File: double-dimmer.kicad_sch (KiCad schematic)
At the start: 4 parts, among them J1 Netzspannung, J2 Screw_Terminal_01x05

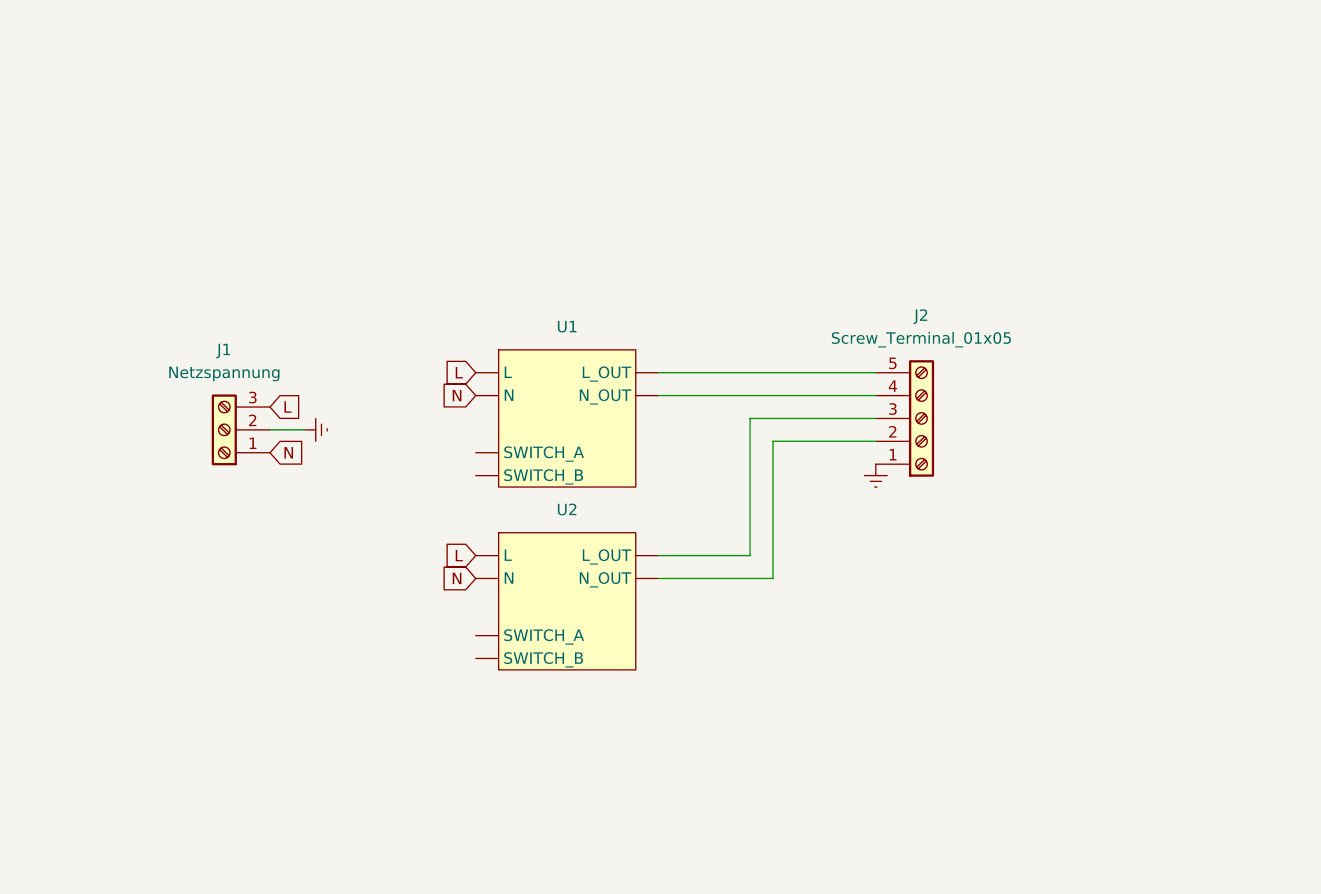
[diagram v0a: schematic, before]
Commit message: Add screenshot and update missing schematic
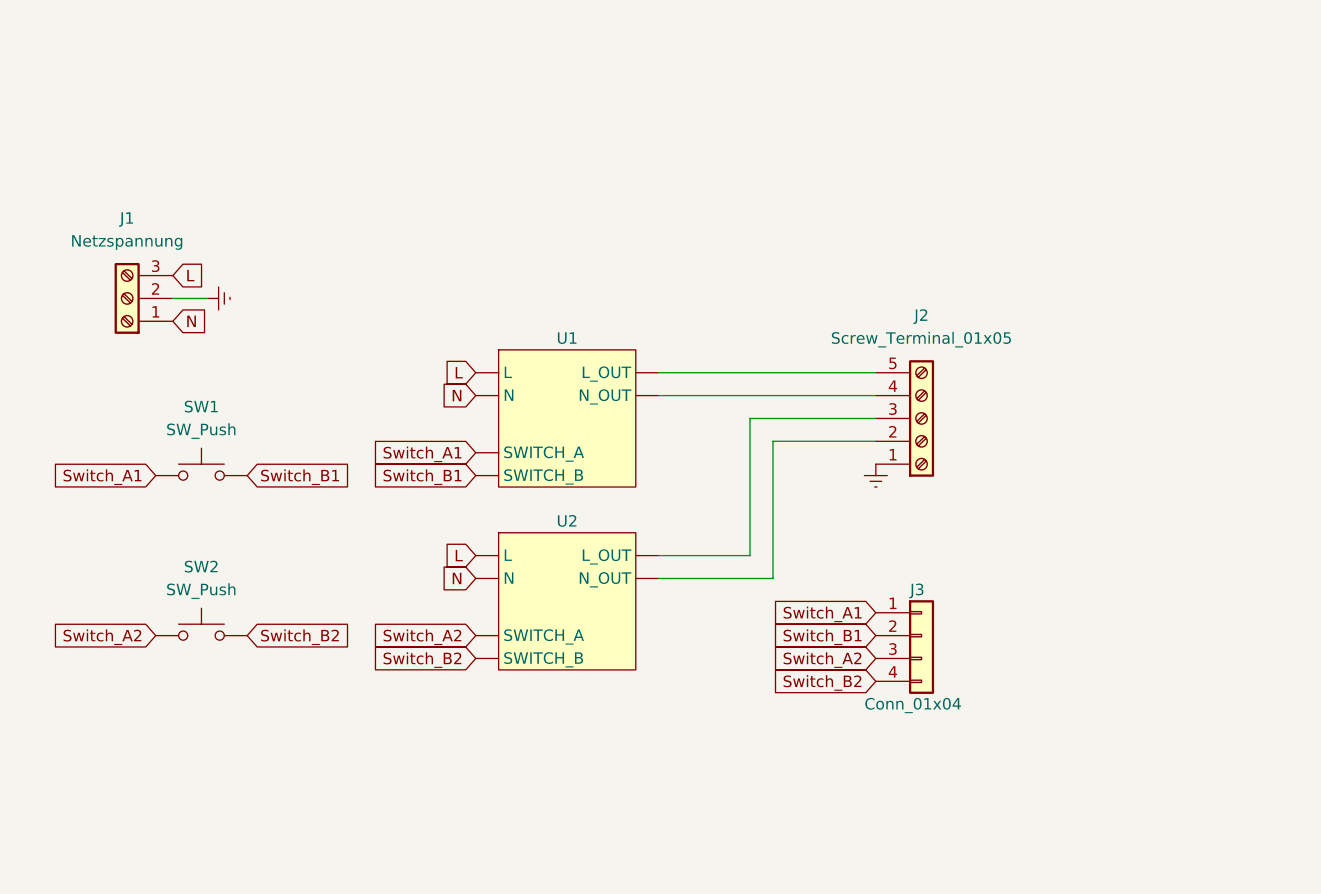
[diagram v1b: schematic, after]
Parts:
- added J3: Conn_01x04, Connector_PinHeader_2.00mm:PinHeader_1x04_P2.00mm_Vertical, symbol Connector_Generic:Conn_01x04
- added SW1, SW2: SW_Push, symbol Switch:SW_Push
- J1: footprint (none) -> TerminalBlock_Phoenix:TerminalBlock_Phoenix_MKDS-1,5-3-5.08_1x03_P5.08mm_Horizontal
- J2: footprint (none) -> TerminalBlock_Phoenix:TerminalBlock_Phoenix_MKDS-1,5-5-5.08_1x05_P5.08mm_Horizontal
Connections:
- net Switch_B2: now reaches U2. (SWITCH_B)
- net Switch_B2: now also J3.4 (Pin_4), SW2.1
- net Switch_B1: now reaches U1. (SWITCH_B)
- net Switch_B1: now also J3.2 (Pin_2), SW1.1
- new net Switch_A1: J3.1 (Pin_1), SW1.2, U1. (SWITCH_B)
- new net Switch_A2: J3.3 (Pin_3), SW2.2, U2. (SWITCH_B)
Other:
- moved on the sheet: J1

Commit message: Update dimmer footprint and add fuse and a switch
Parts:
- added F1: Fuse, Fuse:Fuseholder_Cylinder-5x20mm_Schurter_0031_8201_Horizontal_Open, symbol Device:Fuse
- added SW1: ButtonA, pts636:pts636, symbol Switch:SW_Push
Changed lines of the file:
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@@
+    )
+  )
+  (symbol (lib_id "Device:Fuse") (at 35.56 40.64 90) (unit 1)
+    (in_bom yes) (on_board yes) (dnp no) (fields_autoplaced)
+    (property "Reference" "F1" (at 35.56 34.29 90)
+      (effects (font (size 1.27 1.27)))
+    )
+    (property "Value" "Fuse" (at 35.56 36.83 90)
+      (effects (font (size 1.27 1.27)))
+    )
+    (property "Footprint" "Fuse:Fuseholder_Cylinder-5x20mm_Schurter_0031_8201_Horizontal_Open" (at 35.56 42.418 90)
+      (effects (font (size 1.27 1.27)) hide)
+    )
+    (property "Datasheet" "~" (at 35.56 40.64 0)
+      (effects (font (size 1.27 1.27)) hide)
+    )
+    (property "Price" "2.5" (at 35.56 40.64 0)
+      (effects (font (size 1.27 1.27)) hide)
+    )
+    (property "URL" "" (at 35.56 40.64 0)
+      (effects (font (size 1.27 1.27)) hide)
+    )
+    (pin "1")
+    (pin "2")
+    (instances
+      (project "double-dimmer"
+        (path "/a2cfefb5-9b8f-4ea6-9600-ced2f5c1dc62"
+          (reference "F1") (unit 1)
+        )
+      )
     )
   )
@@
         )
       )
+    )
+  )
+  (symbol (lib_id "Switch:SW_Push") (at 50.8 40.64 0) (unit 1)
+    (in_bom yes) (on_board yes) (dnp no)
+    (property "Reference" "SW1" (at 50.8 36.83 0)
+      (effects (font (size 1.27 1.27)))
+    )
+    (property "Value" "ButtonA" (at 68.58 40.64 0)
+      (effects (font (size 1.27 1.27)) hide)
+    )
+    (property "Footprint" "pts636:pts636" (at 50.8 35.56 0)
+      (effects (font (size 1.27 1.27)) hide)
+    )
+    (property "Datasheet" "~" (at 50.8 35.56 0)
+      (effects (font (size 1.27 1.27)) hide)
+    )
+    (property "Price" ".5" (at 50.8 40.64 0)
+      (effects (font (size 1.27 1.27)) hide)
+    )
+    (property "URL" "https://www.digikey.ch/en/products/detail/c-k/PTS636-SL43-LFS/10071714" (at 50.8 40.64 0)
+      (effects (font (size 1.27 1.27)) hide)
+    )
+    (pin "1")
+    (pin "2")
+    (instances
+      (project "double-dimmer"
+        (path "/a2cfefb5-9b8f-4ea6-9600-ced2f5c1dc62"
+          (reference "SW1") (unit 1)
+        )
+      )

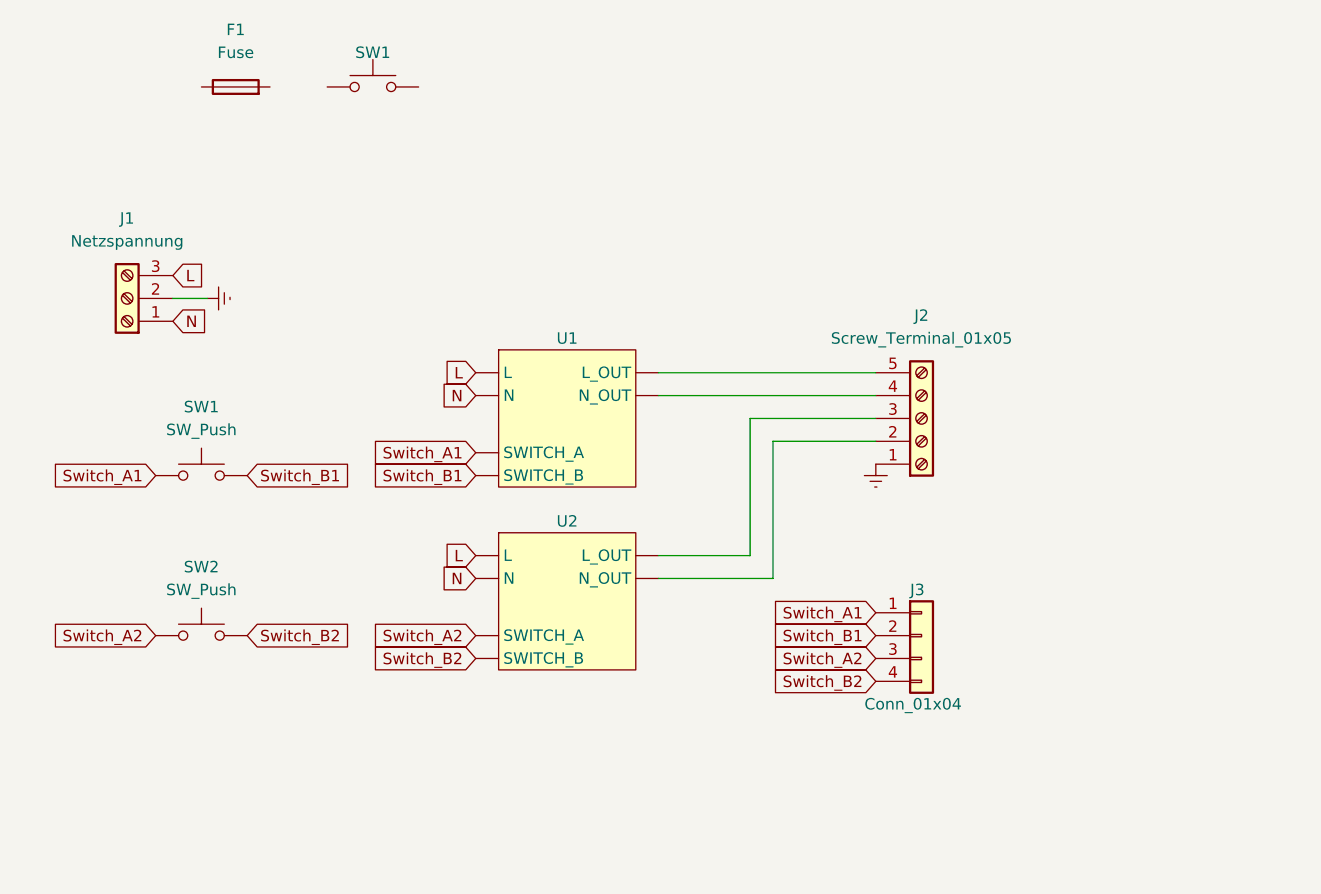
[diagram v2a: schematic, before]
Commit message: Update dimmer footprint and symbol
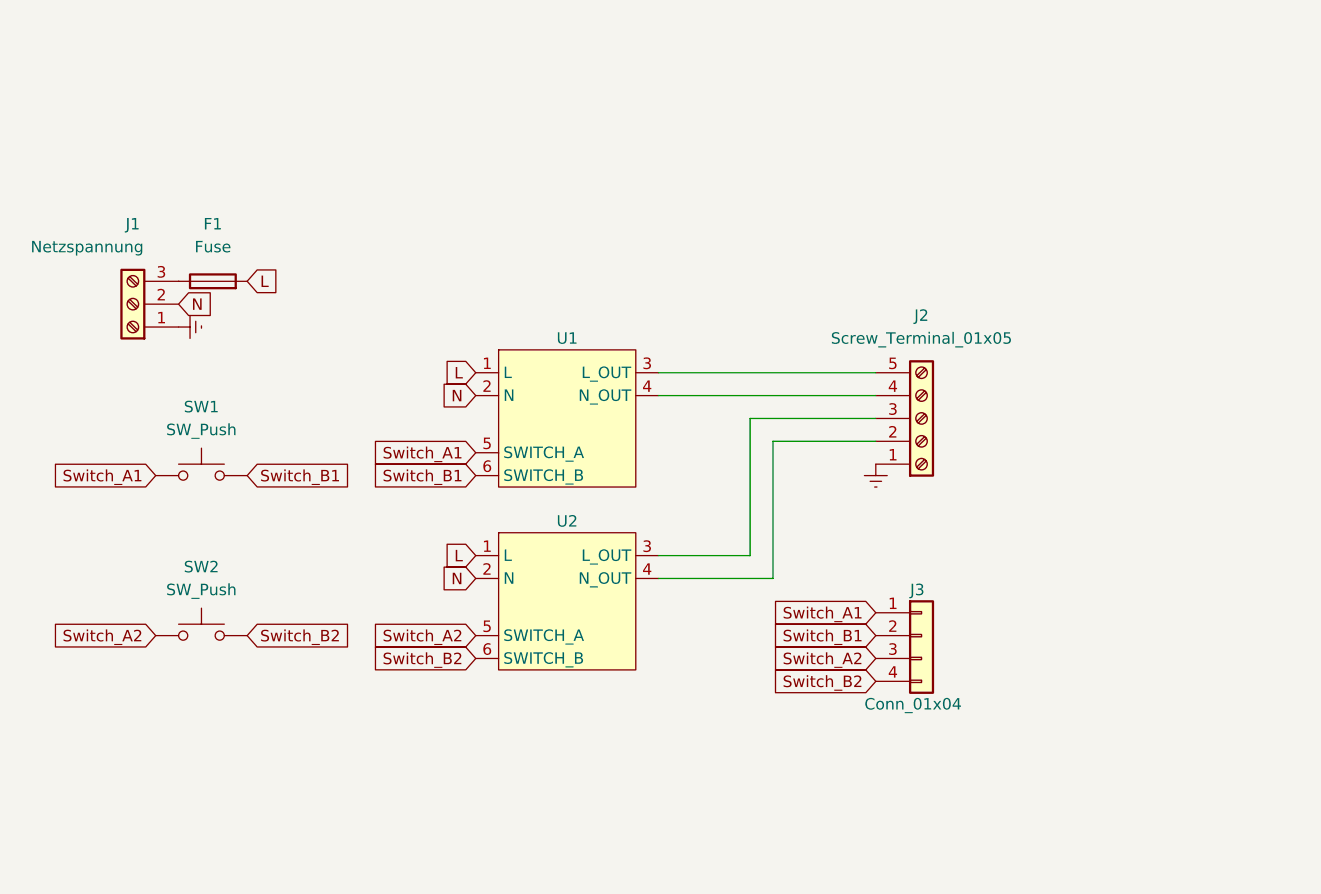
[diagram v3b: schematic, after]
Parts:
- removed SW1: ButtonA, pts636:pts636, symbol Switch:SW_Push
- J3: footprint Connector_PinHeader_2.00mm:PinHeader_1x04_P2.00mm_Vertical -> Connector_PinHeader_2.54mm:PinHeader_1x04_P2.54mm_Vertical
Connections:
- net Earth: now also J1.1 (Pin_1); no longer J1.2 (Pin_2)
- net L: now also F1.2, U1.1 (L), U2.1 (L); no longer J1.3 (Pin_3), U1. (SWITCH_B), U2. (SWITCH_B)
- net N: now also J1.2 (Pin_2), U1.2 (N), U2.2 (N); no longer J1.1 (Pin_1), U1. (SWITCH_B), U2. (SWITCH_B)
- net Switch_A1: now also U1.5 (SWITCH_A); no longer U1. (SWITCH_B)
- net Switch_A2: now also U2.5 (SWITCH_A); no longer U2. (SWITCH_B)
- net Switch_B1: now also U1.6 (SWITCH_B); no longer U1. (SWITCH_B)
- net Switch_B2: now also U2.6 (SWITCH_B); no longer U2. (SWITCH_B)
- net at J2.2 (Pin_2): now also U2.4 (N_OUT); no longer U2. (SWITCH_B)
- net at J2.3 (Pin_3): now also U2.3 (L_OUT); no longer U2. (SWITCH_B)
- net at J2.4 (Pin_4): now also U1.4 (N_OUT); no longer U1. (SWITCH_B)
- net at J2.5 (Pin_5): now also U1.3 (L_OUT); no longer U1. (SWITCH_B)
- net at F1.1: now also J1.3 (Pin_3)
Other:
- moved on the sheet: F1, J1
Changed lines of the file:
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@@
-    (stroke (width 0) (type default))
-  )
-  (wire (pts (xy 32.385 64.135) (xy 28.575 64.135))
     (stroke (width 0) (type default))
   )
@@
     )
   )
-  (global_label "L" (shape input) (at 28.575 61.595 0) (fields_autoplaced)
+  (global_label "L" (shape input) (at 36.83 62.23 0) (fields_autoplaced)
     (effects (font (size 1.27 1.27)) (justify left))
-    (property "Intersheetrefs" "${INTERSHEET_REFS}" (at 32.5883 61.595 0)
+    (property "Intersheetrefs" "${INTERSHEET_REFS}" (at 40.8433 62.23 0)
       (effects (font (size 1.27 1.27)) (justify left) hide)
     )
@@
     )
   )
-  (global_label "N" (shape input) (at 28.575 66.675 0) (fields_autoplaced)
+  (global_label "N" (shape input) (at 29.21 64.77 0) (fields_autoplaced)
     (effects (font (size 1.27 1.27)) (justify left))
-    (property "Intersheetrefs" "${INTERSHEET_REFS}" (at 32.8907 66.675 0)
+    (property "Intersheetrefs" "${INTERSHEET_REFS}" (at 33.5257 64.77 0)
       (effects (font (size 1.27 1.27)) (justify left) hide)
     )
@@
     )
   )
-  (symbol (lib_name "dimmer_1") (lib_id "dimmer:dimmer") (at 72.39 97.79 0) (unit 1)
+  (symbol (lib_id "dimmer:dimmer") (at 72.39 97.79 0) (unit 1)
     (in_bom yes) (on_board yes) (dnp no)
     (property "Reference" "U2" (at 72.39 88.9 0)
@@
       (effects (font (size 1.27 1.27)) hide)
     )
-    (pin "")
-    (pin "")
-    (pin "")
-    (pin "")
-    (pin "")
-    (pin "")
+    (pin "1")
+    (pin "3")
+    (pin "4")
+    (pin "5")
+    (pin "6")
+    (pin "2")
     (instances
       (project "double-dimmer"
@@
       (effects (font (size 1.27 1.27)) hide)
     )
-    (pin "")
-    (pin "")
-    (pin "")
-    (pin "")
-    (pin "")
-    (pin "")
+    (pin "6")
+    (pin "2")
+    (pin "1")
+    (pin "4")
+    (pin "3")
+    (pin "5")
     (instances
       (project "double-dimmer"
@@
     )
   )
-  (symbol (lib_id "Connector:Screw_Terminal_01x03") (at 23.495 64.135 180) (unit 1)
-    (in_bom yes) (on_board yes) (dnp no) (fields_autoplaced)
-    (property "Reference" "J1" (at 23.495 55.245 0)
-      (effects (font (size 1.27 1.27)))
-    )
-    (property "Value" "Netzspannung" (at 23.495 57.785 0)
-      (effects (font (size 1.27 1.27)))
-    )
-    (property "Footprint" "TerminalBlock_Phoenix:TerminalBlock_Phoenix_MKDS-1,5-3-5.08_1x03_P5.08mm_Horizontal" (at 23.495 64.135 0)
-      (effects (font (size 1.27 1.27)) hide)
-    )
-    (property "Datasheet" "~" (at 23.495 64.135 0)
+  (symbol (lib_id "Connector:Screw_Terminal_01x03") (at 24.13 64.77 180) (unit 1)
+    (in_bom yes) (on_board yes) (dnp no)
+    (property "Reference" "J1" (at 24.13 55.88 0)
+      (effects (font (size 1.27 1.27)))
+    )
+    (property "Value" "Netzspannung" (at 19.05 58.42 0)
+      (effects (font (size 1.27 1.27)))
+    )
+    (property "Footprint" "TerminalBlock_Phoenix:TerminalBlock_Phoenix_MKDS-1,5-3-5.08_1x03_P5.08mm_Horizontal" (at 24.13 64.77 0)
+      (effects (font (size 1.27 1.27)) hide)
+    )
+    (property "Datasheet" "~" (at 24.13 64.77 0)
       (effects (font (size 1.27 1.27)) hide)
     )
@@
       (effects (font (size 1.27 1.27)) (justify left))
     )
-    (property "Footprint" "Connector_PinHeader_2.00mm:PinHeader_1x04_P2.00mm_Vertical" (at 111.76 101.6 0)
+    (property "Footprint" "Connector_PinHeader_2.54mm:PinHeader_1x04_P2.54mm_Vertical" (at 111.76 101.6 0)
       (effects (font (size 1.27 1.27)) hide)
     )
@@
     )
   )
-  (symbol (lib_id "Device:Fuse") (at 35.56 40.64 90) (unit 1)
-    (in_bom yes) (on_board yes) (dnp no) (fields_autoplaced)
-    (property "Reference" "F1" (at 35.56 34.29 90)
-      (effects (font (size 1.27 1.27)))
-    )
-    (property "Value" "Fuse" (at 35.56 36.83 90)
-      (effects (font (size 1.27 1.27)))
-    )
-    (property "Footprint" "Fuse:Fuseholder_Cylinder-5x20mm_Schurter_0031_8201_Horizontal_Open" (at 35.56 42.418 90)
-      (effects (font (size 1.27 1.27)) hide)
-    )
-    (property "Datasheet" "~" (at 35.56 40.64 0)
-      (effects (font (size 1.27 1.27)) hide)
-    )
-    (property "Price" "2.5" (at 35.56 40.64 0)
-      (effects (font (size 1.27 1.27)) hide)
-    )
-    (property "URL" "" (at 35.56 40.64 0)
+  (symbol (lib_id "Device:Fuse") (at 33.02 62.23 90) (unit 1)
+    (in_bom yes) (on_board yes) (dnp no) (fields_autoplaced)
+    (property "Reference" "F1" (at 33.02 55.88 90)
+      (effects (font (size 1.27 1.27)))
+    )
+    (property "Value" "Fuse" (at 33.02 58.42 90)
+      (effects (font (size 1.27 1.27)))
+    )
+    (property "Footprint" "Fuse:Fuseholder_Cylinder-5x20mm_Schurter_0031_8201_Horizontal_Open" (at 33.02 64.008 90)
+      (effects (font (size 1.27 1.27)) hide)
+    )
+    (property "Datasheet" "~" (at 33.02 62.23 0)
+      (effects (font (size 1.27 1.27)) hide)
+    )
+    (property "Price" "2.5" (at 33.02 62.23 0)
+      (effects (font (size 1.27 1.27)) hide)
+    )
+    (property "URL" "" (at 33.02 62.23 0)
       (effects (font (size 1.27 1.27)) hide)
     )
@@
   (symbol (lib_id "power:Earth") (at 106.68 82.55 0) (mirror y) (unit 1)
     (in_bom yes) (on_board yes) (dnp no) (fields_autoplaced)
-    (property "Reference" "#PWR04" (at 106.68 88.9 0)
+    (property "Reference" "#PWR02" (at 106.68 88.9 0)
       (effects (font (size 1.27 1.27)) hide)
     )
@@
       (project "double-dimmer"
         (path "/a2cfefb5-9b8f-4ea6-9600-ced2f5c1dc62"
-          (reference "#PWR04") (unit 1)
-        )
-      )
-    )
-  )
-  (symbol (lib_id "power:Earth") (at 32.385 64.135 90) (unit 1)
-    (in_bom yes) (on_board yes) (dnp no) (fields_autoplaced)
-    (property "Reference" "#PWR01" (at 38.735 64.135 0)
-      (effects (font (size 1.27 1.27)) hide)
-    )
-    (property "Value" "Earth" (at 36.195 64.135 0)
-      (effects (font (size 1.27 1.27)) hide)
-    )
-    (property "Footprint" "" (at 32.385 64.135 0)
-      (effects (font (size 1.27 1.27)) hide)
-    )
-    (property "Datasheet" "~" (at 32.385 64.135 0)
+          (reference "#PWR02") (unit 1)
+        )
+      )
+    )
+  )
+  (symbol (lib_id "power:Earth") (at 29.21 67.31 90) (unit 1)
+    (in_bom yes) (on_board yes) (dnp no) (fields_autoplaced)
+    (property "Reference" "#PWR01" (at 35.56 67.31 0)
+      (effects (font (size 1.27 1.27)) hide)
+    )
+    (property "Value" "Earth" (at 33.02 67.31 0)
+      (effects (font (size 1.27 1.27)) hide)
+    )
+    (property "Footprint" "" (at 29.21 67.31 0)
+      (effects (font (size 1.27 1.27)) hide)
+    )
+    (property "Datasheet" "~" (at 29.21 67.31 0)
       (effects (font (size 1.27 1.27)) hide)
     )
@@
         )
       )
-    )
-  )
-  (symbol (lib_id "Switch:SW_Push") (at 50.8 40.64 0) (unit 1)
-    (in_bom yes) (on_board yes) (dnp no)
-    (property "Reference" "SW1" (at 50.8 36.83 0)
-      (effects (font (size 1.27 1.27)))
-    )
-    (property "Value" "ButtonA" (at 68.58 40.64 0)
-      (effects (font (size 1.27 1.27)) hide)
-    )
-    (property "Footprint" "pts636:pts636" (at 50.8 35.56 0)
-      (effects (font (size 1.27 1.27)) hide)
-    )
-    (property "Datasheet" "~" (at 50.8 35.56 0)
-      (effects (font (size 1.27 1.27)) hide)
-    )
-    (property "Price" ".5" (at 50.8 40.64 0)
-      (effects (font (size 1.27 1.27)) hide)
-    )
-    (property "URL" "https://www.digikey.ch/en/products/detail/c-k/PTS636-SL43-LFS/10071714" (at 50.8 40.64 0)
-      (effects (font (size 1.27 1.27)) hide)
-    )
-    (pin "1")
-    (pin "2")
-    (instances
-      (project "double-dimmer"
-        (path "/a2cfefb5-9b8f-4ea6-9600-ced2f5c1dc62"
-          (reference "SW1") (unit 1)
-        )
-      )
